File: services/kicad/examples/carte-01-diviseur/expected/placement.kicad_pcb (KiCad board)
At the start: 2 copper layers, 25 x 20 mm, 5 parts, among them J1 IN

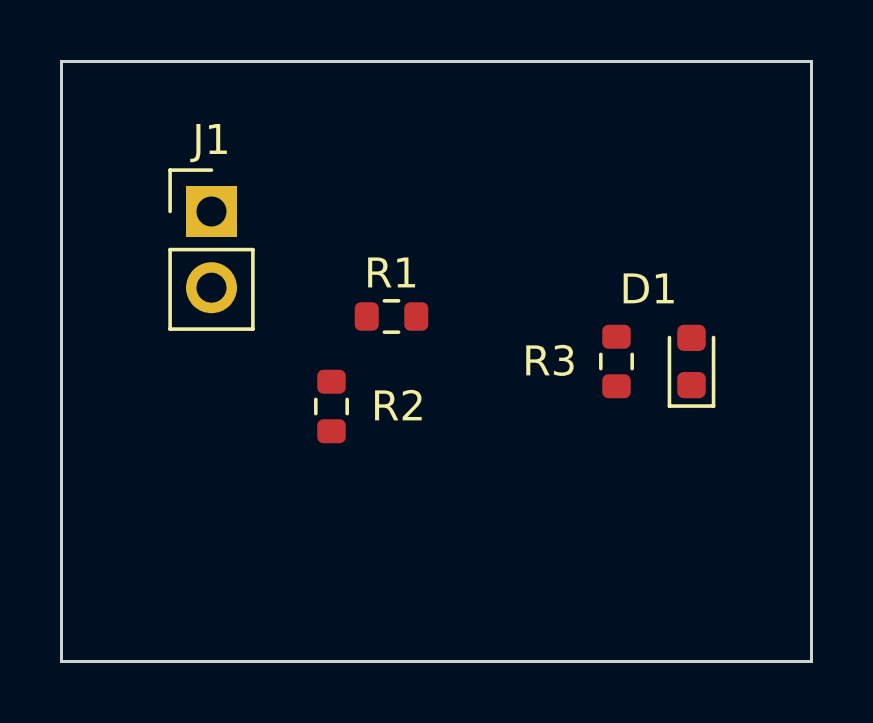
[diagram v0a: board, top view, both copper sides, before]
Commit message: test(examples): quatre cartes livrées plus petites — contour resserré mesuré sur le banc (D-2026-09-13-c A)
Banc rejoué en taille heuristique (phase 1 puis phase 2 à placement gelé) :
carte-01 25x20 -> 24,8x17 (84 % de surface), carte-04 60x45 -> 45x44,8
(75 %), carte-06 80x60 -> 65,2x59,8 (81 %), carte-07 110x80 -> 99,5x79,8
(90 %) — toutes 100 % routées, 0 erreur DRC (vérifié en local), rendus 3D
régénérés. Gain nul sur les cartes denses (le génétique remplit la carte) ;
08 et 09 non livrées (dispersion du routage, surface inchangée) ; carte-11
non livrée (carte d'escalade). Tableau complet dans docs/DECISIONS.md.

Co-Authored-By: Claude Fable 5.1 <noreply@anthropic.com>
Claude-Session: https://claude.ai/code/session_01TnMqm4La2CxQHHB5K8aSSV
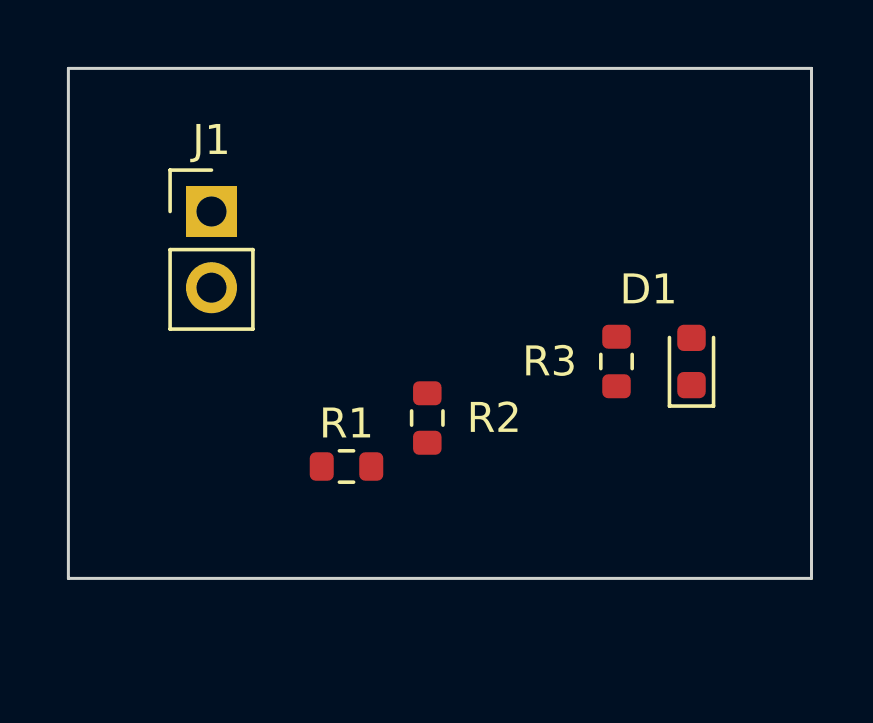
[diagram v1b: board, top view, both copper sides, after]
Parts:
- moved R1 5.22 mm to (145.5, 108.5)
- moved R2 3.22 mm to (148.2, 106.9)
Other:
- board size 25 x 20 mm -> 24.8 x 17 mm
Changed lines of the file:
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@@
 	(title_block
 		(title "Cirqix PCB")
-		(date "2026-09-12")
+		(date "2026-09-13")
 		(rev 1.0)
 		(company "")
@@
 	(net 3 "LED_A")
 	(net 4 "VIN")
-	(gr_rect
-		(start 136 95)
-		(end 161 115)
-		(stroke
-			(width 0.1)
-			(type default)
-		)
-		(fill none)
-		(layer "Edge.Cuts")
-	)
 	(footprint "PinHeader_1x02_P2.54mm_Vertical"
 		(version 20260206)
@@
 		(generator "kicad-footprint-generator")
 		(layer "F.Cu")
-		(at 147 103.5 0)
+		(at 145.5 108.5 0)
 		(descr "Resistor SMD 0603 (1608 Metric), square (rectangular) end terminal, IPC-7351 nominal, (Body size source: IPC-SM-782 page 72, https://www.pcb-3d.com/wordpress/wp-content/uploads/ipc-sm-782a_amendment_1_and_2.pdf)")
 		(tags "resistor")
@@
 		(generator "kicad-footprint-generator")
 		(layer "F.Cu")
-		(at 145 106.5 270)
+		(at 148.1929 106.8842 270)
 		(descr "Resistor SMD 0603 (1608 Metric), square (rectangular) end terminal, IPC-7351 nominal, (Body size source: IPC-SM-782 page 72, https://www.pcb-3d.com/wordpress/wp-content/uploads/ipc-sm-782a_amendment_1_and_2.pdf)")
 		(tags "resistor")
@@
 		)
 	)
+	(gr_rect
+		(start 136.230 95.230)
+		(end 161.000 112.230)
+		(stroke
+			(width 0.1)
+			(type default)
+		)
+		(fill no)
+		(layer "Edge.Cuts")
+	)
 )

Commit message: chore(banc): relivrer carte-01/02/04/05 compactes (25 %, D-2026-09-20-a) (#222)
Chaine place -> route rejouee par HTTP sur les dix cartes avec le code de
#220/#221. Quatre sortent a 0 erreur et 0 connexion manquante, sur des
cartes 18 a 58 % plus petites :

  carte-01  24,8x17 -> 20x14      carte-02  55x40 -> 35x25
  carte-04  45x44,8 -> 39x30      carte-05  70x50 -> 46x33

placement.kicad_pcb et final.kicad_pcb remplaces ENSEMBLE ; mesures.json :
board recompte, drc_du_board rejuge (remesurer_banc.py), cle
carte_compacte (tailles et vias d avant, durees, moteur, pistes par
couche). Rendus refaits. Connecteurs a <= 5 mm d un bord (carte-02 J2 :
13,9 -> 3,8 mm) ; carte-05 J3 inchange a 11,4 mm (origine pin 1).

Les six autres gardent leur board du 2026-09-19 : 06 et 08 a 1 manquante,
03 et 07 mauvais, 09 et 10 sans board (tirages figes). Detail dans
BANC_DRIVER_LLM.md. carte-11 non touchee.


Claude-Session: https://claude.ai/code/session_01TnMqm4La2CxQHHB5K8aSSV

Co-authored-by: Claude Fable 5.1 <noreply@anthropic.com>
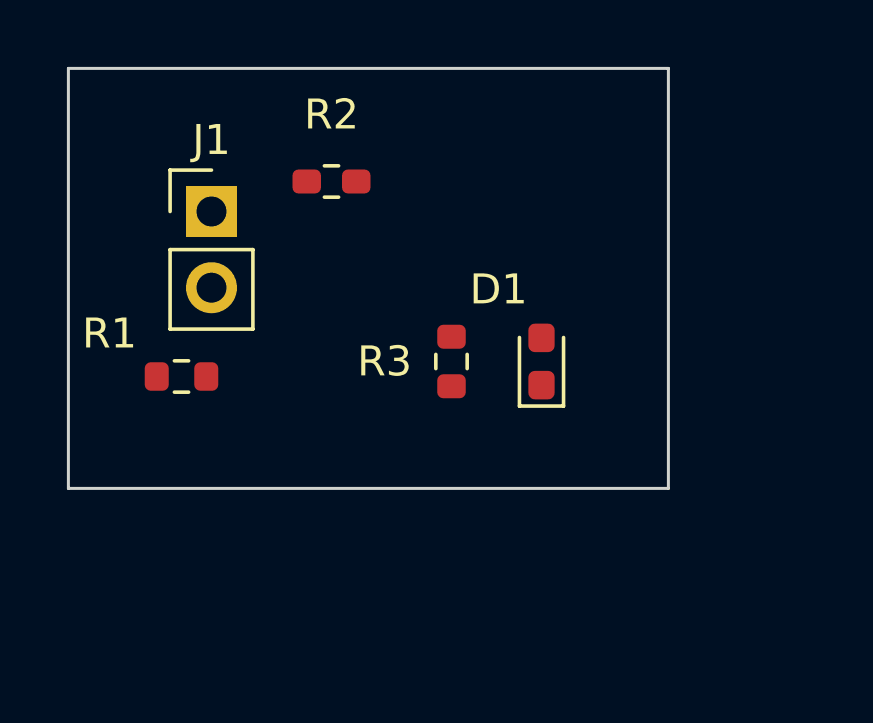
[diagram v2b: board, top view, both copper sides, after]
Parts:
- moved R2 8.51 mm to (145.0, 99.0), turned to 0 degrees
- moved R1 6.26 mm to (140.0, 105.5)
- moved R3 5.50 mm to (149.0, 105.0)
- moved D1 5.00 mm to (152.0, 105.0)
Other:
- board size 24.8 x 17 mm -> 20 x 14 mm
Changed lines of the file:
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@@
 		(generator "kicad-footprint-generator")
 		(layer "F.Cu")
-		(at 145.5 108.5 0)
+		(at 140 105.5 0)
 		(descr "Resistor SMD 0603 (1608 Metric), square (rectangular) end terminal, IPC-7351 nominal, (Body size source: IPC-SM-782 page 72, https://www.pcb-3d.com/wordpress/wp-content/uploads/ipc-sm-782a_amendment_1_and_2.pdf)")
 		(tags "resistor")
 		(property "Reference" "R1"
-			(at 0 -1.43 0)
+			(at -2.4 -1.43 0)
 			(layer "F.SilkS")
 			(effects
@@
 		(generator "kicad-footprint-generator")
 		(layer "F.Cu")
-		(at 148.1929 106.8842 270)
+		(at 145 99 0)
 		(descr "Resistor SMD 0603 (1608 Metric), square (rectangular) end terminal, IPC-7351 nominal, (Body size source: IPC-SM-782 page 72, https://www.pcb-3d.com/wordpress/wp-content/uploads/ipc-sm-782a_amendment_1_and_2.pdf)")
 		(tags "resistor")
@@
 		(generator "kicad-footprint-generator")
 		(layer "F.Cu")
-		(at 154.5 105 90)
+		(at 149 105 90)
 		(descr "Resistor SMD 0603 (1608 Metric), square (rectangular) end terminal, IPC-7351 nominal, (Body size source: IPC-SM-782 page 72, https://www.pcb-3d.com/wordpress/wp-content/uploads/ipc-sm-782a_amendment_1_and_2.pdf)")
 		(tags "resistor")
@@
 		(generator "kicad-footprint-generator")
 		(layer "F.Cu")
-		(at 157 105 90)
+		(at 152 105 90)
 		(descr "LED SMD 0603 (1608 Metric), square (rectangular) end terminal, IPC-7351 nominal, (Body size source: http://www.tortai-tech.com/upload/download/2011102023233369053.pdf)")
 		(tags "LED")
@@
 		)
 		(pad "1" smd roundrect
-			(at -0.7875 0 90)
+			(at -0.7875 0 180)
 			(size 0.875 0.95)
 			(layers "F.Cu" "F.Mask" "F.Paste")
@@
 		)
 		(pad "2" smd roundrect
-			(at 0.7875 0 90)
+			(at 0.7875 0 180)
 			(size 0.875 0.95)
 			(layers "F.Cu" "F.Mask" "F.Paste")
@@
 	(gr_rect
 		(start 136.230 95.230)
-		(end 161.000 112.230)
+		(end 156.230 109.230)
 		(stroke
 			(width 0.1)

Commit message: fix(kicad): plan de masse referme — banc DIX cartes sur dix, 0 erreur 0 manquante (#237)
* docs(kicad): la derniere rupture de plan tient a UN segment, pas a un faisceau

Diagnostic complet du seul defaut restant du banc (carte-10), mesure sur le
board qui le porte vraiment, apres consultation de Codex et de GLM.

Mesures sur `/tmp/livr/carte-10-maximale/route.kicad_pcb` (33 violations,
0 erreur, 1 connexion manquante) :

- 23 ilots GND sur les deux faces, exactement 2 orphelins, et ce sont des
  JUMEAUX : F.Cu 1,30 mm2 (porte la pastille C35.2) et B.Cu 0,99 mm2.
- AUCUN de leurs points n a le plan principal en vis-a-vis : ils se font face
  l un l autre. La piste « changer de face par un via », proposee par GLM, est
  donc REFUTEE par la mesure.
- La couture de production visite les deux ilots et refuse la totalite de
  leurs sites (23 et 18 candidats ; obstacle 16/10, hors_polygone 6/7,
  trou_trop_pres 1/1) : un via ne tient pas dans un millimetre carre.
  Le raccord par courte piste rend relies 0, sans_chemin 19.
- Mais le plan principal n est qu a 0,862 mm sur F.Cu et 0,781 mm sur B.Cu, et
  UN SEUL segment coupe le couloir de chaque face (EXT2_1, EXT4_1).

Le plan de Codex — deplacer l obstacle au lieu de chercher un passage a
travers — a donc ici un ensemble a arracher d UN segment par face, pas une
recherche ouverte. Decision de strategie de routage : D-2026-09-22-a, EN
ATTENTE. Rien n est implemente.

Levier natif verifie et jamais appele : LocalRerouter.reroute_segment() de
kicad-tools, utilise par drc/repair_clearance.py, zero appelant Cirqix. Il
travaille sur le document S-expression quand notre code travaille sur pcbnew.

Lecons inscrites dans CLAUDE.md :
- j ai d abord mesure le board VERSIONNE du 21, qui est propre (non_connectes
  0) et se pretait a toutes les demonstrations — un via y tenait avec 0,29 mm
  de marge. Verifier que l artefact PORTE le defaut avant de le diagnostiquer.
- ma premiere sonde raisonnait zone par zone, alors que la carte por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
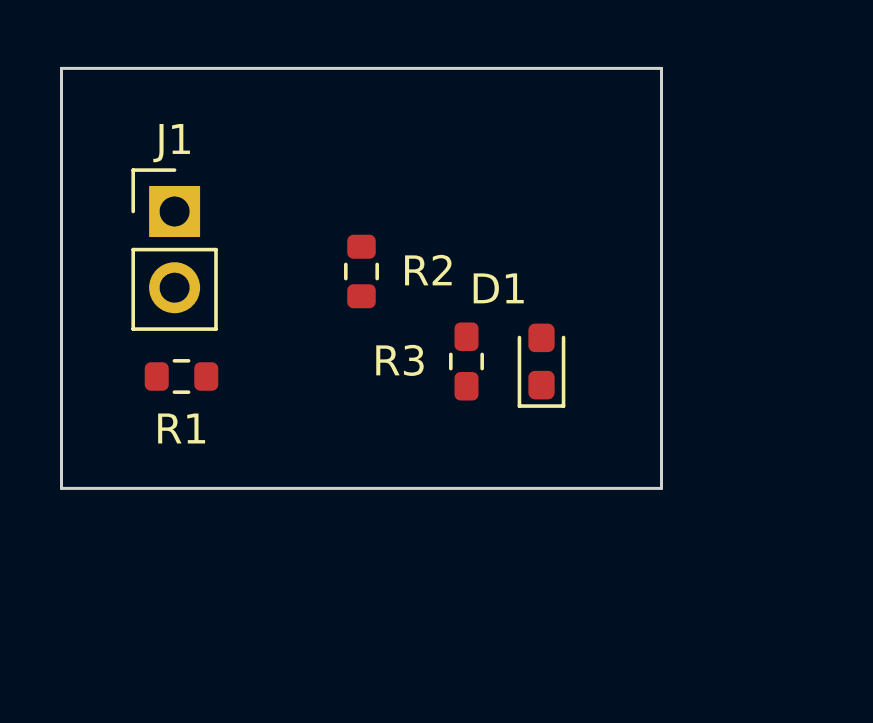
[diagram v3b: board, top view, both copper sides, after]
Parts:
- moved R2 3.16 mm to (146.0, 102.0), turned to 270 degrees
- moved J1 1.23 mm to (139.8, 100.0)
- moved R3 0.50 mm to (149.5, 105.0)
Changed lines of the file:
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@@
 (kicad_pcb
-	(version 20260206)
+	(version 20241229)
 	(generator "kicad_tools")
 	(generator_version "10.0")
@@
 	(title_block
 		(title "Cirqix PCB")
-		(date "2026-09-13")
+		(date "2026-09-23")
 		(rev 1.0)
 		(company "")
@@
 		(generator "kicad-footprint-generator")
 		(layer "F.Cu")
-		(at 141 100 0)
+		(at 139.77 100 0)
 		(descr "Through hole straight pin header, 1x02, 2.54mm pitch, single row")
 		(tags "Through hole pin header THT 1x02 2.54mm single row")
@@
 		(tags "resistor")
 		(property "Reference" "R1"
-			(at -2.4 -1.43 0)
+			(at 1.95943e-16 1.77 0)
 			(layer "F.SilkS")
 			(effects
@@
 		(generator "kicad-footprint-generator")
 		(layer "F.Cu")
-		(at 145 99 0)
+		(at 146 102 270)
 		(descr "Resistor SMD 0603 (1608 Metric), square (rectangular) end terminal, IPC-7351 nominal, (Body size source: IPC-SM-782 page 72, https://www.pcb-3d.com/wordpress/wp-content/uploads/ipc-sm-782a_amendment_1_and_2.pdf)")
 		(tags "resistor")
@@
 		(generator "kicad-footprint-generator")
 		(layer "F.Cu")
-		(at 149 105 90)
+		(at 149.5 105 90)
 		(descr "Resistor SMD 0603 (1608 Metric), square (rectangular) end terminal, IPC-7351 nominal, (Body size source: IPC-SM-782 page 72, https://www.pcb-3d.com/wordpress/wp-content/uploads/ipc-sm-782a_amendment_1_and_2.pdf)")
 		(tags "resistor")
@@
 		)
 		(pad "1" smd roundrect
-			(at -0.825 0 90)
+			(at -0.825 0)
 			(size 0.8 0.95)
 			(layers "F.Cu" "F.Mask" "F.Paste")
@@
 		)
 		(pad "2" smd roundrect
-			(at 0.825 0 90)
+			(at 0.825 0)
 			(size 0.8 0.95)
 			(layers "F.Cu" "F.Mask" "F.Paste")
@@
 		)
 		(pad "1" smd roundrect
-			(at -0.7875 0 180)
+			(at -0.7875 0)
 			(size 0.875 0.95)
 			(layers "F.Cu" "F.Mask" "F.Paste")
@@
 		)
 		(pad "2" smd roundrect
-			(at 0.7875 0 180)
+			(at 0.7875 0)
 			(size 0.875 0.95)
 			(layers "F.Cu" "F.Mask" "F.Paste")
@@
 	)
 	(gr_rect
-		(start 136.230 95.230)
-		(end 156.230 109.230)
+		(start 136.000 95.230)
+		(end 156.000 109.230)
 		(stroke
 			(width 0.1)
